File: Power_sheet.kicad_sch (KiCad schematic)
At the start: 27 parts, among them J1 Jack-DC, Q1 SS8050, SW1 SW_SPDT, U2 HT7333

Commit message: update -- i don't remeber what
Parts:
- C14, C15, C16, C17, C18, C19, C20, C21: footprint (none) -> Capacitor_SMD:C_0805_2012Metric
- R23, R24, R25, R26, R27, R28: footprint (none) -> Resistor_SMD:R_0805_2012Metric
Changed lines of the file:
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@@
 			)
 		)
-		(property "Footprint" ""
+		(property "Footprint" "Capacitor_SMD:C_0805_2012Metric"
 			(at 67.6148 116.84 0)
 			(effects
@@
 			)
 		)
-		(property "Footprint" ""
+		(property "Footprint" "Resistor_SMD:R_0805_2012Metric"
 			(at 52.832 52.07 90)
 			(effects
@@
 			)
 		)
-		(property "Footprint" ""
+		(property "Footprint" "Capacitor_SMD:C_0805_2012Metric"
 			(at 123.19 153.9748 0)
 			(effects
@@
 			)
 		)
-		(property "Footprint" ""
+		(property "Footprint" "Capacitor_SMD:C_0805_2012Metric"
 			(at 44.7548 156.21 0)
 			(effects
@@
 			)
 		)
-		(property "Footprint" ""
+		(property "Footprint" "Capacitor_SMD:C_0805_2012Metric"
 			(at 56.1848 156.21 0)
 			(effects
@@
 			)
 		)
-		(property "Footprint" ""
+		(property "Footprint" "Capacitor_SMD:C_0805_2012Metric"
 			(at 105.7148 74.93 0)
 			(effects
@@
 			)
 		)
-		(property "Footprint" ""
+		(property "Footprint" "Capacitor_SMD:C_0805_2012Metric"
 			(at 94.2848 74.93 0)
 			(effects
@@
 			)
 		)
-		(property "Footprint" ""
+		(property "Footprint" "Resistor_SMD:R_0805_2012Metric"
 			(at 78.74 44.958 90)
 			(effects
@@
 			)
 		)
-		(property "Footprint" ""
+		(property "Footprint" "Resistor_SMD:R_0805_2012Metric"
 			(at 65.532 167.64 90)
 			(effects
@@
 			)
 		)
-		(property "Footprint" ""
+		(property "Footprint" "Resistor_SMD:R_0805_2012Metric"
 			(at 65.532 152.4 90)
 			(effects
@@
 			)
 		)
-		(property "Footprint" ""
+		(property "Footprint" "Resistor_SMD:R_0805_2012Metric"
 			(at 119.38 111.252 90)
 			(effects
@@
 			)
 		)
-		(property "Footprint" ""
+		(property "Footprint" "Capacitor_SMD:C_0805_2012Metric"
 			(at 32.7152 163.83 0)
 			(effects
@@
 			)
 		)
-		(property "Footprint" ""
+		(property "Footprint" "Resistor_SMD:R_0805_2012Metric"
 			(at 18.542 38.1 90)
 			(effects
@@
 			)
 		)
-		(property "Footprint" ""
+		(property "Footprint" "Capacitor_SMD:C_0805_2012Metric"
 			(at 79.0448 116.84 0)
 			(effects

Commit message: moved firmware development to a different folder
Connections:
- net GND: now also SW1.1 (A)
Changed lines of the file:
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@@
+	)
+	(symbol
+		(lib_id "power:GND")
+		(at 77.47 77.47 270)
+		(unit 1)
+		(exclude_from_sim no)
+		(in_bom yes)
+		(on_board yes)
+		(dnp no)
+		(fields_autoplaced yes)
+		(property "Reference" "#PWR031"
+			(at 71.12 77.47 0)
+			(effects
+				(font
+					(size 1.27 1.27)
+				)
+				(hide yes)
+			)
+		)
+		(property "Value" "GND"
+			(at 73.66 77.4699 90)
+			(effects
+				(font
+					(size 1.27 1.27)
+				)
+				(justify right)
+			)
+		)
+		(property "Footprint" ""
+			(at 77.47 77.47 0)
+			(effects
+				(font
+					(size 1.27 1.27)
+				)
+				(hide yes)
+			)
+		)
+		(property "Datasheet" ""
+			(at 77.47 77.47 0)
+			(effects
+				(font
+					(size 1.27 1.27)
+				)
+				(hide yes)
+			)
+		)
+		(property "Description" "Power symbol creates a global label with name \"GND\" , ground"
+			(at 77.47 77.47 0)
+			(effects
+				(font
+					(size 1.27 1.27)
+				)
+				(hide yes)
+			)
+		)
+		(pin "1"
+		)
+		(instances
+			(project "miniHexa"
+				(path "/3449ee66-2977-4802-a474-0821cdf4e79b/33698118-31e2-44d0-a5be-b46ca646d44a"
+					(reference "#PWR031")
+					(unit 1)
+				)
+			)
+		)
 	)
 	(symbol

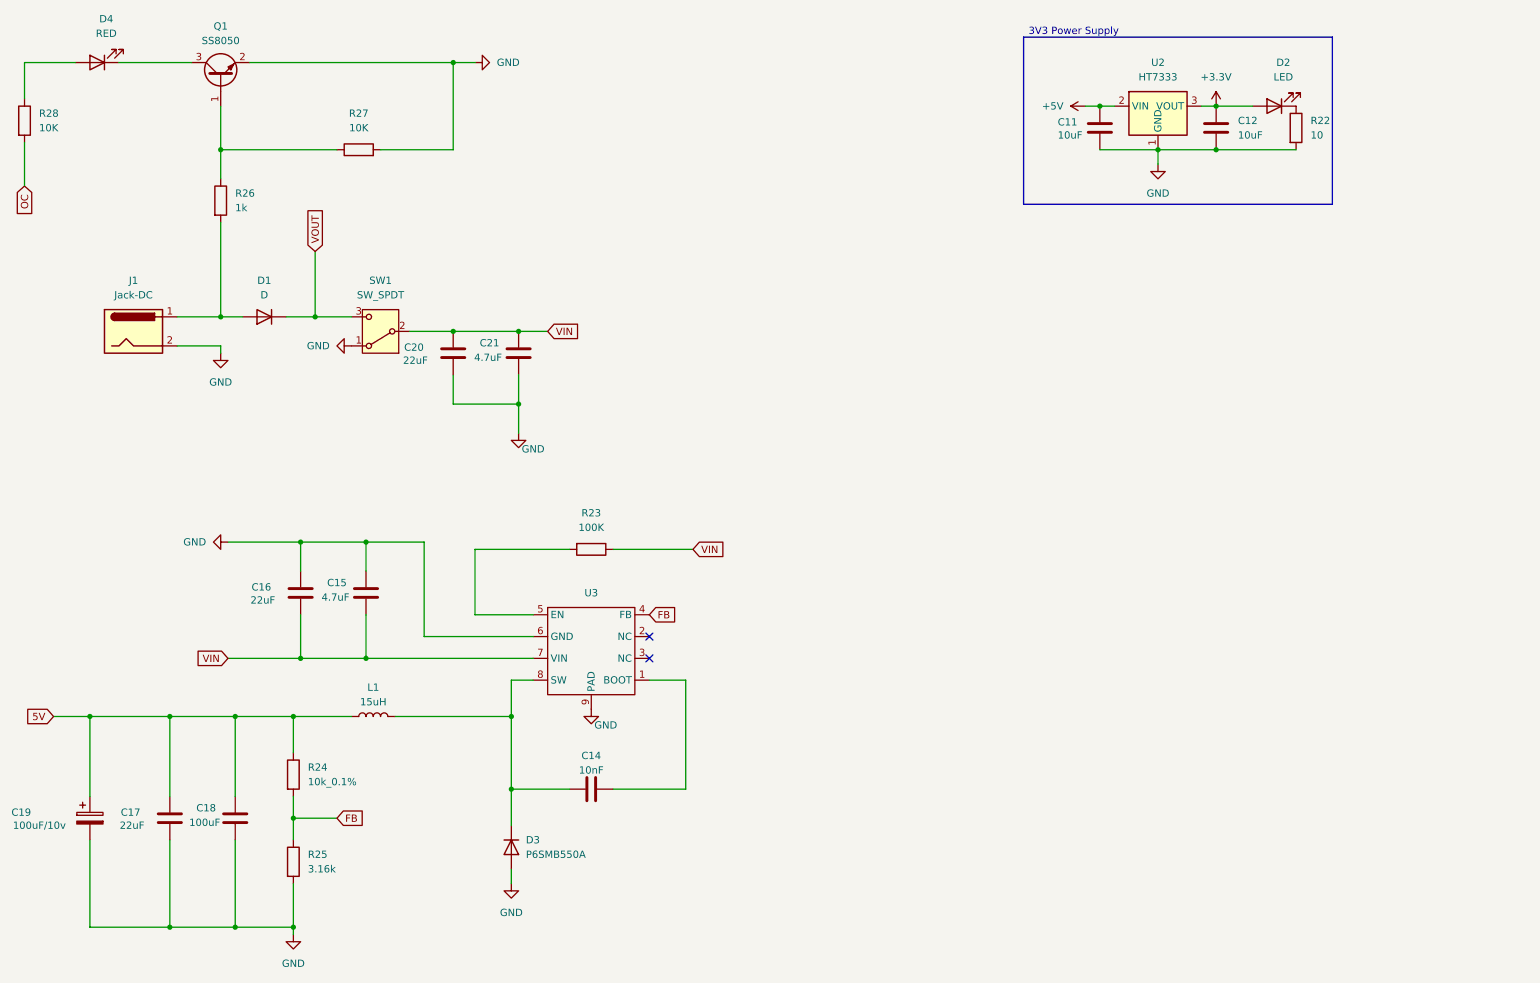
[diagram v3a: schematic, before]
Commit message: assigned footprints and I2c for stm32
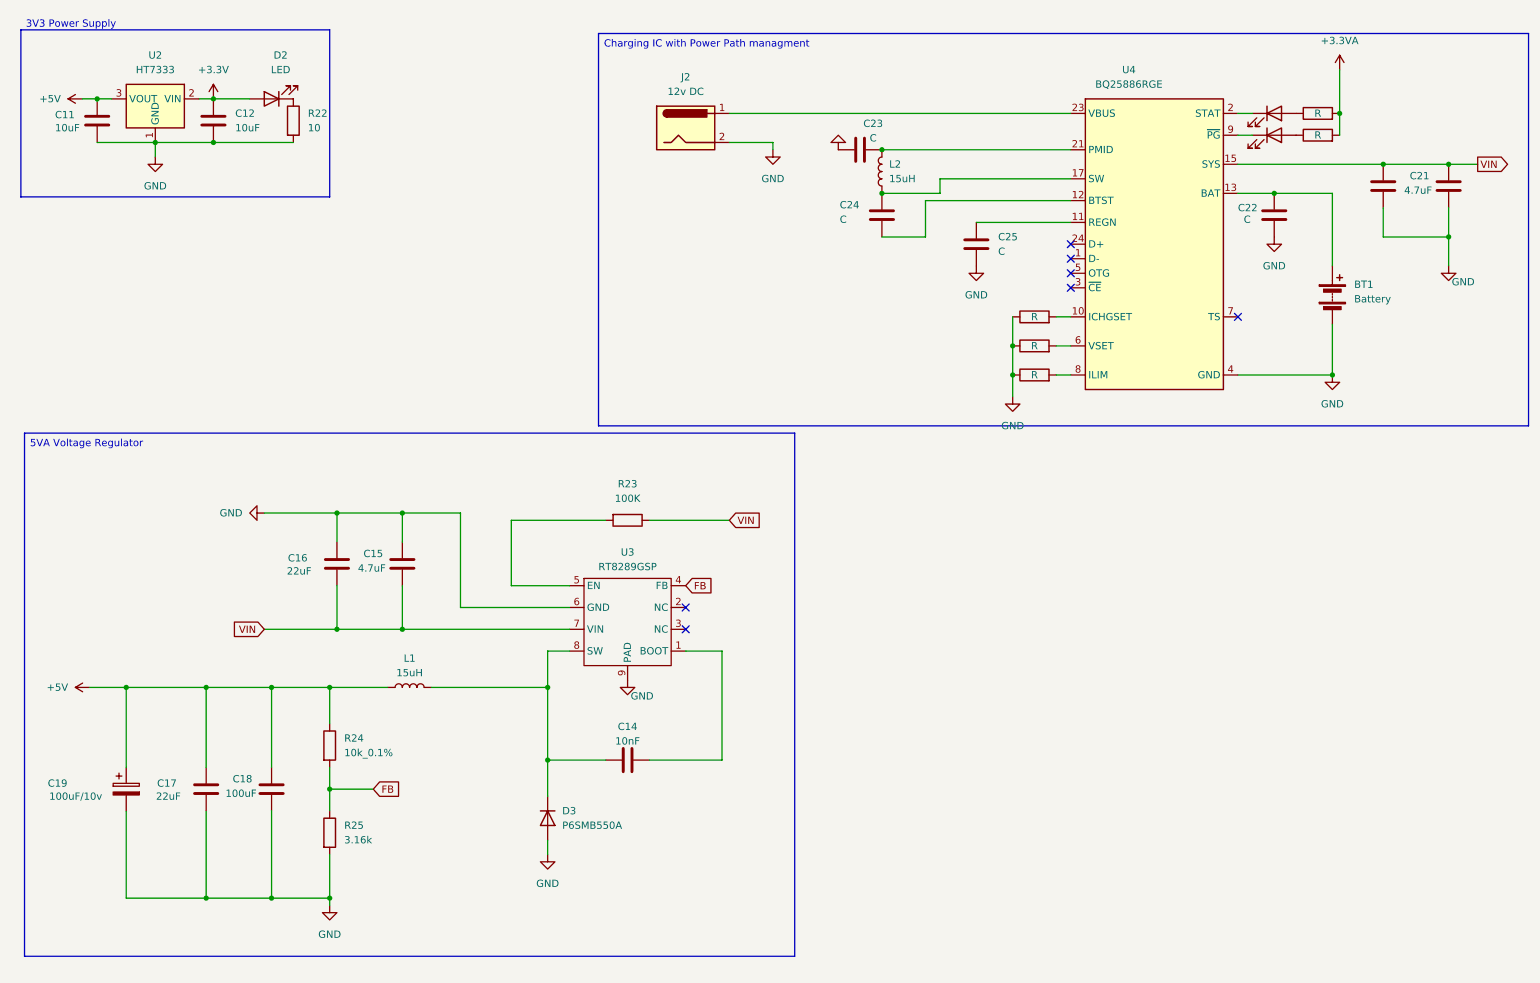
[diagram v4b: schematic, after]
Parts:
- removed D1: D, Diode_SMD:D_0805_2012Metric_Pad1.15x1.40mm_HandSolder, symbol Device:D
- removed J1: Jack-DC, symbol Connector:Jack-DC
- removed Q1: SS8050, Package_TO_SOT_SMD:SOT-23, symbol Transistor_BJT:SS8050
- removed SW1: SW_SPDT, symbol Switch:SW_SPDT
- added BT1: Battery, symbol Device:Battery
- added C22, C23, C24, C25: C, Capacitor_SMD:C_0805_2012Metric, symbol Device:C
- added D5: LED, LED_SMD:LED_0805_2012Metric, symbol Device:LED
- added J2: 12v DC, Connector_BarrelJack:BarrelJack_Wuerth_694102107102_1.0x3.9mm, symbol Connector:Jack-DC
- added L2: 15uH, Inductor_SMD:L_APV_APH0850, symbol Device:L
- added R30, R31: R, Resistor_SMD:R_0805_2012Metric, symbol Device:R
- added U4: BQ25886RGE, Package_DFN_QFN:Texas_RGE0024H_VQFN-24-1EP_4x4mm_P0.5mm_EP2.7x2.7mm, symbol Battery_Management:BQ25886RGE
- D3: footprint (none) -> Diode_SMD:D_0805_2012Metric_Pad1.15x1.40mm_HandSolder
- D4: value RED -> LED; footprint (none) -> LED_SMD:LED_0805_2012Metric
- L1: footprint (none) -> Inductor_SMD:L_APV_APH0850
- R26: value 1k -> R
- R27, R28: value 10K -> R
- U3: value ~ -> RT8289GSP
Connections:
- net 5V is gone; now on net +5V: C17.2, C18.2, C19.1, L1.1, R24.1
- net +3.3V: now also U2.2 (VIN); no longer U2.3 (VOUT)
- net +5V: now also U2.3 (VOUT); no longer U2.2 (VIN)
- net GND: now also R26.1, BT1.2 (-), C22.2, C23.1, C25.2, J2.2, R30.1, R31.1, U4.19 (GND), U4.20 (GND), U4.25 (GND), U4.4 (GND); no longer R27.2
- net VIN: now also U4.15 (SYS), U4.16 (SYS)
- net at R27.1: now also D4.2 (A); no longer R26.1
- net at R26.2: now also U4.10 (ICHGSET)
- net at D4.1 (K): now also U4.2 (STAT)
- net at R28.1: now also D5.2 (A); no longer D4.2 (A)
- net OC renamed +3.3VA
- net +3.3VA: now also R27.2
- new net: J2.1, U4.23 (VBUS)
- new net: C25.1, U4.11 (REGN)
- new net: C24.2, U4.12 (BTST)
- new net: BT1.1 (+), C22.1, U4.13 (BAT), U4.14 (BAT)
- new net: C24.1, L2.1, U4.17 (SW), U4.18 (SW)
- new net: C23.2, L2.2, U4.21 (PMID), U4.22 (PMID)
- new net: R30.2, U4.6 (VSET)
- new net: R31.2, U4.8 (ILIM)
- new net: D5.1 (K), U4.9 (~{PG})
- no-connect marks 2 -> 7
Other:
- moved on the sheet: C11, C12, C14, C15, C16, C17, C18, C19, C21, D2, D3, L1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

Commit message: Removed redundent components
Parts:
- BT1: footprint (none) -> Battery:BatteryHolder_Keystone_2468_2xAAA
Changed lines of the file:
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@@
 			)
 		)
-		(property "Footprint" ""
+		(property "Footprint" "Battery:BatteryHolder_Keystone_2468_2xAAA"
 			(at 248.92 67.056 90)
 			(effects
